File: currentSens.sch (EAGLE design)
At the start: 21 parts, among them U2 ATMEGA328P_TQFP

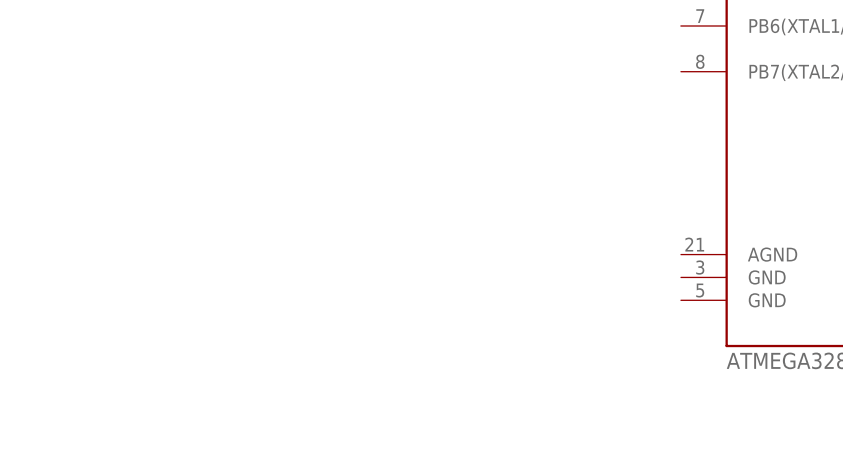
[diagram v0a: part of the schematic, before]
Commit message: included the MCP3008 current sensors and traces
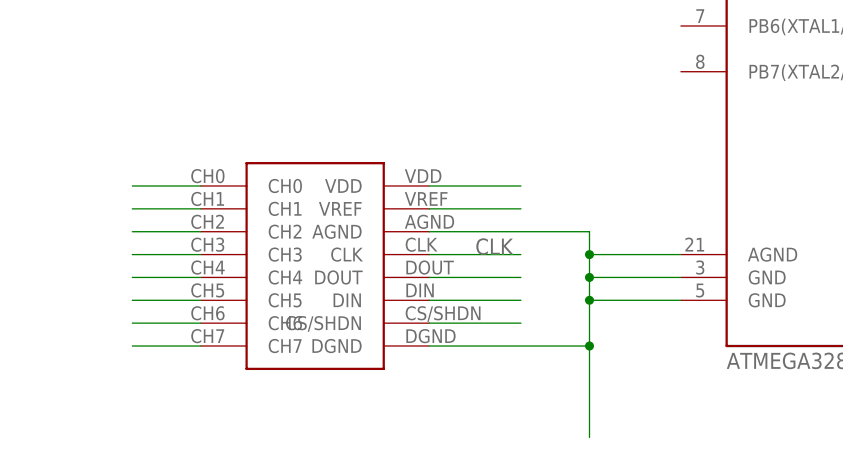
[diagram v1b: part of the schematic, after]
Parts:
- added U$1: MCP3008, MCP3008:MCP3008
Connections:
- new net CH0: U$1.CH0
- new net CH1: U$1.CH1
- new net CH2: U$1.CH2
- new net CH3: U$1.CH3
- new net CH4: U$1.CH4
- new net CH5: U$1.CH5
- new net CH6: U$1.CH6
- new net CH7: U$1.CH7
- new net CLK: U$1.CLK
- new net CS/SHDN: U$1.CS/SHDN
- new net DIN: U$1.DIN
- new net DOUT: U$1.DOUT
- new net N$1: U$1.AGND, U$1.DGND, U2.AGND, U2.GND@3, U2.GND@5
- new net VDD: U$1.VDD
- new net VREF: U$1.VREF
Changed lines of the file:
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@@
 <layers>
 <layer number="1" name="Top" color="4" fill="1" visible="no" active="no"/>
+<layer number="2" name="Route2" color="1" fill="3" visible="no" active="no"/>
+<layer number="3" name="Route3" color="4" fill="3" visible="no" active="no"/>
+<layer number="4" name="Route4" color="1" fill="4" visible="no" active="no"/>
+<layer number="5" name="Route5" color="4" fill="4" visible="no" active="no"/>
+<layer number="6" name="Route6" color="1" fill="8" visible="no" active="no"/>
+<layer number="7" name="Route7" color="4" fill="8" visible="no" active="no"/>
+<layer number="8" name="Route8" color="1" fill="2" visible="no" active="no"/>
+<layer number="9" name="Route9" color="4" fill="2" visible="no" active="no"/>
+<layer number="10" name="Route10" color="1" fill="7" visible="no" active="no"/>
+<layer number="11" name="Route11" color="4" fill="7" visible="no" active="no"/>
+<layer number="12" name="Route12" color="1" fill="5" visible="no" active="no"/>
+<layer number="13" name="Route13" color="4" fill="5" visible="no" active="no"/>
+<layer number="14" name="Route14" color="1" fill="6" visible="no" active="no"/>
+<layer number="15" name="Route15" color="4" fill="6" visible="no" active="no"/>
 <layer number="16" name="Bottom" color="1" fill="1" visible="no" active="no"/>
 <layer number="17" name="Pads" color="2" fill="1" visible="no" active="no"/>
@@
 <part name="GND19" library="supply1" library_urn="urn:adsk.eagle:library:371" deviceset="GND" device=""/>
 <part name="GND20" library="supply1" library_urn="urn:adsk.eagle:library:371" deviceset="GND" device=""/>
+<part name="U$1" library="MCP3008" deviceset="MCP3008" device=""/>
 </parts>
 <sheets>
@@
 <instance part="GND19" gate="1" x="114.3" y="256.54"/>
 <instance part="GND20" gate="1" x="104.14" y="261.62"/>
+<instance part="U$1" gate="G$1" x="53.34" y="101.6"/>
 </instances>
 <busses>
@@
 </segment>
 </net>
+<net name="CLK" class="0">
+<segment>
+<pinref part="U$1" gate="G$1" pin="CLK"/>
+<wire x1="68.58" y1="99.06" x2="78.74" y2="99.06" width="0.1524" layer="91"/>
+<label x="73.66" y="99.06" size="1.778" layer="95"/>
+</segment>
+</net>
+<net name="N$1" class="0">
+<segment>
+<pinref part="U$1" gate="G$1" pin="AGND"/>
+<wire x1="68.58" y1="101.6" x2="86.36" y2="101.6" width="0.1524" layer="91"/>
+<wire x1="86.36" y1="101.6" x2="86.36" y2="99.06" width="0.1524" layer="91"/>
+<pinref part="U$1" gate="G$1" pin="DGND"/>
+<wire x1="86.36" y1="99.06" x2="86.36" y2="96.52" width="0.1524" layer="91"/>
+<wire x1="86.36" y1="96.52" x2="86.36" y2="93.98" width="0.1524" layer="91"/>
+<wire x1="86.36" y1="93.98" x2="86.36" y2="88.9" width="0.1524" layer="91"/>
+<wire x1="86.36" y1="88.9" x2="86.36" y2="78.74" width="0.1524" layer="91"/>
+<wire x1="68.58" y1="88.9" x2="86.36" y2="88.9" width="0.1524" layer="91"/>
+<junction x="86.36" y="88.9"/>
+<pinref part="U2" gate="U$1" pin="AGND"/>
+<wire x1="96.52" y1="99.06" x2="86.36" y2="99.06" width="0.1524" layer="91"/>
+<junction x="86.36" y="99.06"/>
+<pinref part="U2" gate="U$1" pin="GND@3"/>
+<wire x1="96.52" y1="96.52" x2="86.36" y2="96.52" width="0.1524" layer="91"/>
+<junction x="86.36" y="96.52"/>
+<pinref part="U2" gate="U$1" pin="GND@5"/>
+<wire x1="96.52" y1="93.98" x2="86.36" y2="93.98" width="0.1524" layer="91"/>
+<junction x="86.36" y="93.98"/>
+</segment>
+</net>
+<net name="VREF" class="0">
+<segment>
+<pinref part="U$1" gate="G$1" pin="VREF"/>
+<wire x1="68.58" y1="104.14" x2="78.74" y2="104.14" width="0.1524" layer="91"/>
+</segment>
+</net>
+<net name="VDD" class="0">
+<segment>
+<pinref part="U$1" gate="G$1" pin="VDD"/>
+<wire x1="68.58" y1="106.68" x2="78.74" y2="106.68" width="0.1524" layer="91"/>
+</segment>
+</net>
+<net name="CH0" class="0">
+<segment>
+<pinref part="U$1" gate="G$1" pin="CH0"/>
+<wire x1="43.18" y1="106.68" x2="35.56" y2="106.68" width="0.1524" layer="91"/>
+</segment>
+</net>
+<net name="CH1" class="0">
+<segment>
+<pinref part="U$1" gate="G$1" pin="CH1"/>
+<wire x1="43.18" y1="104.14" x2="35.56" y2="104.14" width="0.1524" layer="91"/>
+</segment>
+</net>
+<net name="CH2" class="0">
+<segment>
+<pinref part="U$1" gate="G$1" pin="CH2"/>
+<wire x1="43.18" y1="101.6" x2="35.56" y2="101.6" width="0.1524" layer="91"/>
+</segment>
+</net>
+<net name="CH3" class="0">
+<segment>
+<pinref part="U$1" gate="G$1" pin="CH3"/>
+<wire x1="43.18" y1="99.06" x2="35.56" y2="99.06" width="0.1524" layer="91"/>
+</segment>
+</net>
+<net name="CH4" class="0">
+<segment>
+<pinref part="U$1" gate="G$1" pin="CH4"/>
+<wire x1="43.18" y1="96.52" x2="35.56" y2="96.52" width="0.1524" layer="91"/>
+</segment>
+</net>
+<net name="CH5" class="0">
+<segment>
+<pinref part="U$1" gate="G$1" pin="CH5"/>
+<wire x1="43.18" y1="93.98" x2="35.56" y2="93.98" width="0.1524" layer="91"/>
+</segment>
+</net>
+<net name="CH6" class="0">
+<segment>
+<pinref part="U$1" gate="G$1" pin="CH6"/>
+<wire x1="43.18" y1="91.44" x2="35.56" y2="91.44" width="0.1524" layer="91"/>
+</segment>
+</net>
+<net name="CH7" class="0">
+<segment>
+<pinref part="U$1" gate="G$1" pin="CH7"/>
+<wire x1="43.18" y1="88.9" x2="35.56" y2="88.9" width="0.1524" layer="91"/>
+</segment>
+</net>
+<net name="DOUT" class="0">
+<segment>
+<pinref part="U$1" gate="G$1" pin="DOUT"/>
+<wire x1="68.58" y1="96.52" x2="78.74" y2="96.52" width="0.1524" layer="91"/>
+</segment>
+</net>
+<net name="DIN" class="0">
+<segment>
+<pinref part="U$1" gate="G$1" pin="DIN"/>
+<wire x1="68.58" y1="93.98" x2="78.74" y2="93.98" width="0.1524" layer="91"/>
+</segment>
+</net>
+<net name="CS/SHDN" class="0">
+<segment>
+<pinref part="U$1" gate="G$1" pin="CS/SHDN"/>
+<wire x1="68.58" y1="91.44" x2="78.74" y2="91.44" width="0.1524" layer="91"/>
+</segment>
+</net>
